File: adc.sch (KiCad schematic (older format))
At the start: 86 parts, among them J1 Conn_02x08_Odd_Even, J2 Conn_02x08_Odd_Even, J3 Conn_02x08_Odd_Even, J4 Conn_02x08_Odd_Even, J5 Conn_01x04_Male, J9 Conn_02x08_Odd_Even, U1 ADC128D818, U2 ADC128D818, U3 ADC128D818, U4 ADC128D818, U5 ADC128D818

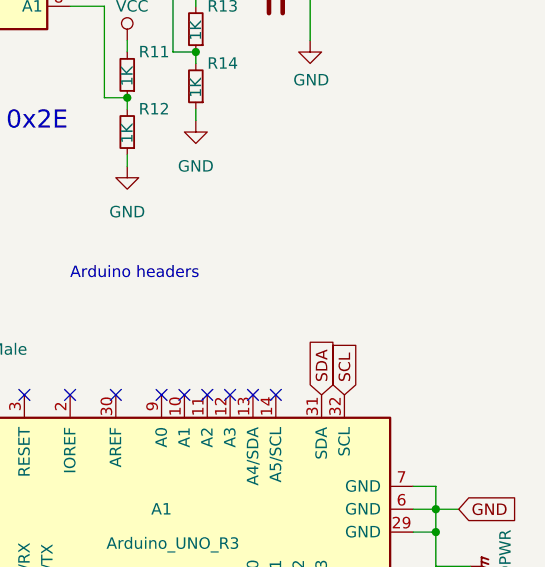
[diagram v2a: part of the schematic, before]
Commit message: add i2c pullup resistors
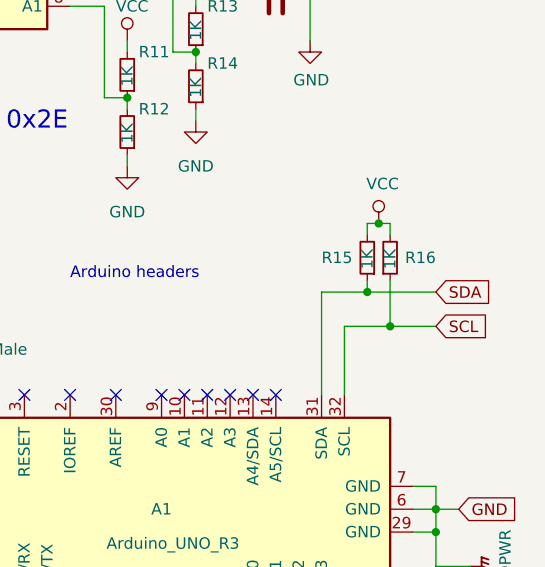
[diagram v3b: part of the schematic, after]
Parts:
- added R15, R16: 1K, Resistor_SMD:R_0805_2012Metric_Pad1.15x1.40mm_HandSolder, symbol Device:R_Small
- C1, C10, C13, C15, C17, C19, C2, C5, C7, C9: footprint Capacitor_Tantalum_SMD:CP_EIA-6032-28_Kemet-C_Pad2.25x2.35mm_HandSolder -> Capacitor_Tantalum_SMD:CP_EIA-3216-18_Kemet-A_Pad1.58x1.35mm_HandSolder
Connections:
- net SCL: now also R16.1
- net SDA: now also R15.1
- net VCC: now also R15.2, R16.2
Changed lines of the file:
@@
 	7400 5150 7400 5250
 Connection ~ 7400 5250
-Text GLabel 10300 4950 1    50   Input ~ 0
+Text GLabel 10800 4500 2    50   Input ~ 0
 SDA
-Text GLabel 10400 4950 1    50   Input ~ 0
+Text GLabel 10800 4650 2    50   Input ~ 0
 SCL
 $Comp
@@
 F 0 "C13" V 6650 5700 50  0000 L CNN
 F 1 "1U TANT C" V 6550 5400 50  0000 L CNN
-F 2 "Capacitor_Tantalum_SMD:CP_EIA-6032-28_Kemet-C_Pad2.25x2.35mm_HandSolder" H 6588 5900 50  0001 C CNN
+F 2 "Capacitor_Tantalum_SMD:CP_EIA-3216-18_Kemet-A_Pad1.58x1.35mm_HandSolder" H 6588 5900 50  0001 C CNN
 F 3 "~" H 6550 6050 50  0001 C CNN
 	1    6550 6050
@@
 F 0 "C9" H 4450 4300 50  0000 L CNN
 F 1 "1U TANT C" H 4400 4200 50  0000 L CNN
-F 2 "Capacitor_Tantalum_SMD:CP_EIA-6032-28_Kemet-C_Pad2.25x2.35mm_HandSolder" H 4938 4100 50  0001 C CNN
+F 2 "Capacitor_Tantalum_SMD:CP_EIA-3216-18_Kemet-A_Pad1.58x1.35mm_HandSolder" H 4938 4100 50  0001 C CNN
 F 3 "~" H 4900 4250 50  0001 C CNN
 	1    4900 4250
@@
 F 0 "C5" V 3100 6300 50  0000 L CNN
 F 1 "1U TANT C" V 3000 6000 50  0000 L CNN
-F 2 "Capacitor_Tantalum_SMD:CP_EIA-6032-28_Kemet-C_Pad2.25x2.35mm_HandSolder" H 3038 6500 50  0001 C CNN
+F 2 "Capacitor_Tantalum_SMD:CP_EIA-3216-18_Kemet-A_Pad1.58x1.35mm_HandSolder" H 3038 6500 50  0001 C CNN
 F 3 "~" H 3000 6650 50  0001 C CNN
 	1    3000 6650
@@
 F 0 "C1" H 900 4900 50  0000 L CNN
 F 1 "1U TANT C" H 850 4800 50  0000 L CNN
-F 2 "Capacitor_Tantalum_SMD:CP_EIA-6032-28_Kemet-C_Pad2.25x2.35mm_HandSolder" H 1388 4700 50  0001 C CNN
+F 2 "Capacitor_Tantalum_SMD:CP_EIA-3216-18_Kemet-A_Pad1.58x1.35mm_HandSolder" H 1388 4700 50  0001 C CNN
 F 3 "~" H 1350 4850 50  0001 C CNN
 	1    1350 4850
@@
 F 0 "C7" V 3500 2800 50  0000 L CNN
 F 1 "1U TANT C" V 3400 2500 50  0000 L CNN
-F 2 "Capacitor_Tantalum_SMD:CP_EIA-6032-28_Kemet-C_Pad2.25x2.35mm_HandSolder" H 3438 3000 50  0001 C CNN
+F 2 "Capacitor_Tantalum_SMD:CP_EIA-3216-18_Kemet-A_Pad1.58x1.35mm_HandSolder" H 3438 3000 50  0001 C CNN
 F 3 "~" H 3400 3150 50  0001 C CNN
 	1    3400 3150
@@
 F 0 "C2" H 1300 1400 50  0000 L CNN
 F 1 "1U TANT C" H 1250 1300 50  0000 L CNN
-F 2 "Capacitor_Tantalum_SMD:CP_EIA-6032-28_Kemet-C_Pad2.25x2.35mm_HandSolder" H 1788 1200 50  0001 C CNN
+F 2 "Capacitor_Tantalum_SMD:CP_EIA-3216-18_Kemet-A_Pad1.58x1.35mm_HandSolder" H 1788 1200 50  0001 C CNN
 F 3 "~" H 1750 1350 50  0001 C CNN
 	1    1750 1350
@@
 F 0 "C19" V 10200 2600 50  0000 L CNN
 F 1 "1U TANT C" V 10100 2300 50  0000 L CNN
-F 2 "Capacitor_Tantalum_SMD:CP_EIA-6032-28_Kemet-C_Pad2.25x2.35mm_HandSolder" H 10138 2800 50  0001 C CNN
+F 2 "Capacitor_Tantalum_SMD:CP_EIA-3216-18_Kemet-A_Pad1.58x1.35mm_HandSolder" H 10138 2800 50  0001 C CNN
 F 3 "~" H 10100 2950 50  0001 C CNN
 	1    10100 2950
@@
 F 0 "C17" H 8000 1200 50  0000 L CNN
 F 1 "1U TANT C" H 7950 1100 50  0000 L CNN
-F 2 "Capacitor_Tantalum_SMD:CP_EIA-6032-28_Kemet-C_Pad2.25x2.35mm_HandSolder" H 8488 1000 50  0001 C CNN
+F 2 "Capacitor_Tantalum_SMD:CP_EIA-3216-18_Kemet-A_Pad1.58x1.35mm_HandSolder" H 8488 1000 50  0001 C CNN
 F 3 "~" H 8450 1150 50  0001 C CNN
 	1    8450 1150
@@
 F 0 "C15" V 6950 2600 50  0000 L CNN
 F 1 "1U TANT C" V 6850 2300 50  0000 L CNN
-F 2 "Capacitor_Tantalum_SMD:CP_EIA-6032-28_Kemet-C_Pad2.25x2.35mm_HandSolder" H 6888 2800 50  0001 C CNN
+F 2 "Capacitor_Tantalum_SMD:CP_EIA-3216-18_Kemet-A_Pad1.58x1.35mm_HandSolder" H 6888 2800 50  0001 C CNN
 F 3 "~" H 6850 2950 50  0001 C CNN
 	1    6850 2950
@@
 F 0 "C10" H 4750 1200 50  0000 L CNN
 F 1 "1U TANT C" H 4700 1100 50  0000 L CNN
-F 2 "Capacitor_Tantalum_SMD:CP_EIA-6032-28_Kemet-C_Pad2.25x2.35mm_HandSolder" H 5238 1000 50  0001 C CNN
+F 2 "Capacitor_Tantalum_SMD:CP_EIA-3216-18_Kemet-A_Pad1.58x1.35mm_HandSolder" H 5238 1000 50  0001 C CNN
 F 3 "~" H 5200 1150 50  0001 C CNN
 	1    5200 1150
@@
 NoConn ~ 9100 5950
 NoConn ~ 9000 5950
+$Comp
+L Device:R_Small R15
+U 1 1 5C4E408F
+P 10500 4350
+F 0 "R15" H 10700 4350 50  0000 R CNN
+F 1 "1K" V 10500 4400 50  0000 R CNN
+F 2 "Resistor_SMD:R_0805_2012Metric_Pad1.15x1.40mm_HandSolder" H 10500 4350 50  0001 C CNN
+F 3 "~" H 10500 4350 50  0001 C CNN
+	1    10500 4350
+	-1   0    0    1
+$EndComp
+Wire Wire Line
+	10400 4650 10600 4650
+Wire Wire Line
+	10800 4500 10500 4500
+Wire Wire Line
+	10400 4650 10400 4950
+Wire Wire Line
+	10300 4500 10300 4950
+$Comp
+L power:VCC #PWR044
+U 1 1 5C63A4BA
+P 10550 4200
+F 0 "#PWR044" H 10550 4050 50  0001 C CNN
+F 1 "VCC" H 10567 4373 50  0000 C CNN
+F 2 "" H 10550 4200 50  0001 C CNN
+F 3 "" H 10550 4200 50  0001 C CNN
+	1    10550 4200
+	1    0    0    -1
+$EndComp
+$Comp
+L Device:R_Small R16
+U 1 1 5C63AD89
+P 10600 4350
+F 0 "R16" H 10800 4350 50  0000 R CNN
+F 1 "1K" V 10600 4400 50  0000 R CNN
+F 2 "Resistor_SMD:R_0805_2012Metric_Pad1.15x1.40mm_HandSolder" H 10600 4350 50  0001 C CNN
+F 3 "~" H 10600 4350 50  0001 C CNN
+	1    10600 4350
+	1    0    0    1
+$EndComp
+Wire Wire Line
+	10500 4450 10500 4500
+Connection ~ 10500 4500
+Wire Wire Line
+	10500 4500 10300 4500
+Wire Wire Line
+	10600 4450 10600 4650
+Connection ~ 10600 4650
+Wire Wire Line
+	10600 4650 10800 4650
+Wire Wire Line
+	10550 4200 10500 4200
+Wire Wire Line
+	10500 4200 10500 4250
+Wire Wire Line
+	10550 4200 10600 4200
+Wire Wire Line
+	10600 4200 10600 4250
+Connection ~ 10550 4200
 $EndSCHEMATC

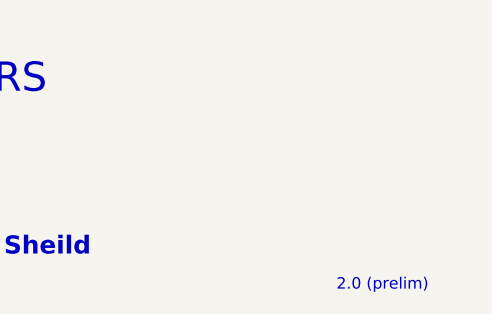
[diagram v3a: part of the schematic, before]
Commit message: mark schematic as V2 final
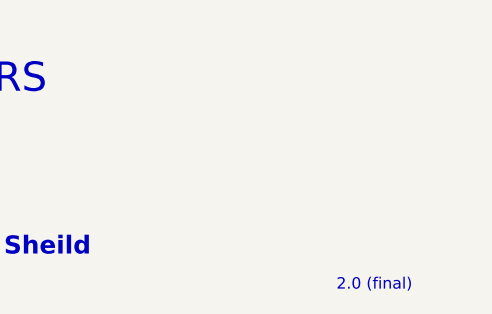
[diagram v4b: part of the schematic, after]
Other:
- note added: "2.0 (final)"
- note removed: "2.0 (prelim)"
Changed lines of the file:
@@
 2018 Nov 29
 Text Notes 10600 7650 0    50   ~ 0
-2.0 (prelim)
+2.0 (final)
 Text Notes 7000 7000 0    128  ~ 0
 Property  of Team OTheRS\nJacob Killelea

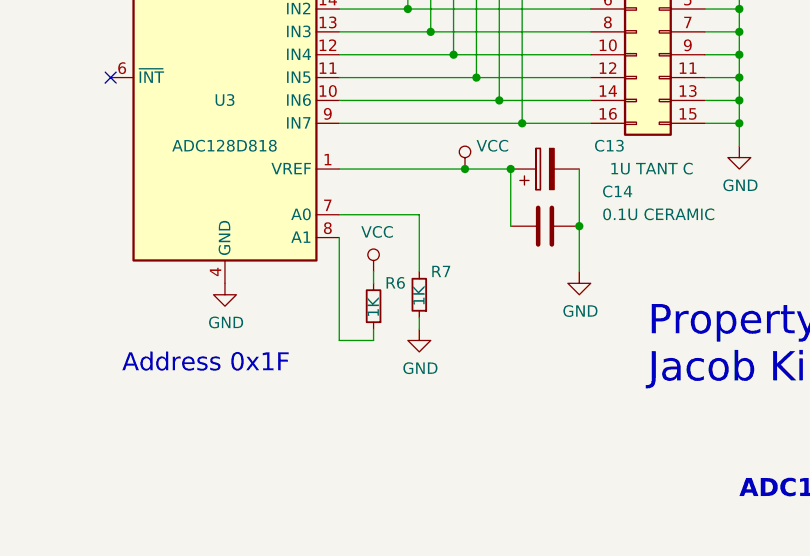
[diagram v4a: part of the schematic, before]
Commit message: update trace width after ITLL CNC cutting and correct error causing chip 0x1F to show up as 0x35
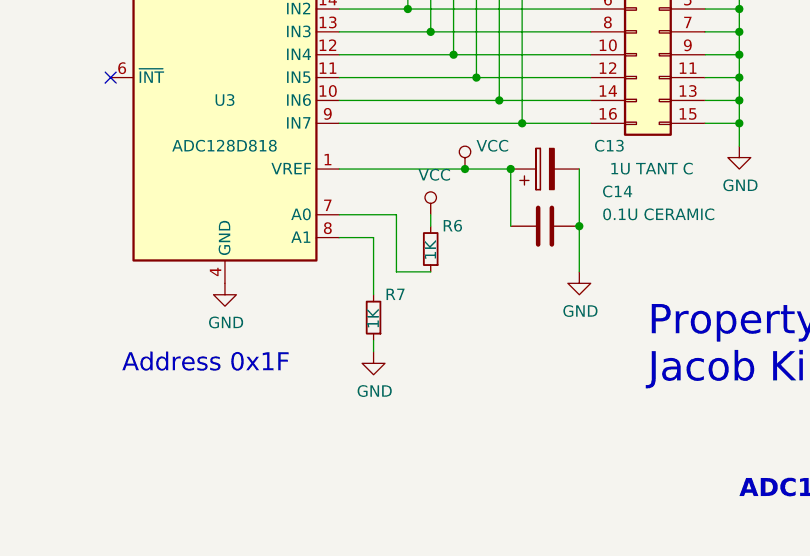
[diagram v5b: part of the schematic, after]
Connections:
- net at U3.7 (A0): now also R6.1; no longer R7.2
- net at U3.8 (A1): now also R7.2; no longer R6.1
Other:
- moved on the sheet: R6, R7
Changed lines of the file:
@@
 L Device:R_Small R7
 U 1 1 5CDACB2D
-P 6000 6600
-F 0 "R7" H 5950 6500 50  0000 R CNN
-F 1 "1K" V 6000 6650 50  0000 R CNN
-F 2 "Resistor_SMD:R_0805_2012Metric_Pad1.15x1.40mm_HandSolder" H 6000 6600 50  0001 C CNN
-F 3 "~" H 6000 6600 50  0001 C CNN
-	1    6000 6600
+P 5800 6700
+F 0 "R7" H 5750 6600 50  0000 R CNN
+F 1 "1K" V 5800 6750 50  0000 R CNN
+F 2 "Resistor_SMD:R_0805_2012Metric_Pad1.15x1.40mm_HandSolder" H 5800 6700 50  0001 C CNN
+F 3 "~" H 5800 6700 50  0001 C CNN
+	1    5800 6700
 	-1   0    0    1
 $EndComp
@@
 L power:GND #PWR016
 U 1 1 5C457890
-P 6000 6750
-F 0 "#PWR016" H 6000 6500 50  0001 C CNN
-F 1 "GND" H 6005 6577 50  0000 C CNN
-F 2 "" H 6000 6750 50  0001 C CNN
-F 3 "" H 6000 6750 50  0001 C CNN
-	1    6000 6750
-	1    0    0    -1
-$EndComp
-Wire Wire Line
-	6000 6700 6000 6750
-Wire Wire Line
-	5650 6250 6000 6250
-Wire Wire Line
-	6000 6250 6000 6500
+P 5800 6850
+F 0 "#PWR016" H 5800 6600 50  0001 C CNN
+F 1 "GND" H 5805 6677 50  0000 C CNN
+F 2 "" H 5800 6850 50  0001 C CNN
+F 3 "" H 5800 6850 50  0001 C CNN
+	1    5800 6850
+	1    0    0    -1
+$EndComp
+Wire Wire Line
+	5800 6800 5800 6850
 $Comp
 L power:VCC #PWR012
 U 1 1 5C4B3FE4
-P 5800 6500
-F 0 "#PWR012" H 5800 6350 50  0001 C CNN
-F 1 "VCC" H 5817 6673 50  0000 C CNN
-F 2 "" H 5800 6500 50  0001 C CNN
-F 3 "" H 5800 6500 50  0001 C CNN
-	1    5800 6500
+P 6050 6250
+F 0 "#PWR012" H 6050 6100 50  0001 C CNN
+F 1 "VCC" H 6067 6423 50  0000 C CNN
+F 2 "" H 6050 6250 50  0001 C CNN
+F 3 "" H 6050 6250 50  0001 C CNN
+	1    6050 6250
 	1    0    0    -1
 $EndComp
@@
 L Device:R_Small R6
 U 1 1 5C4B413F
-P 5800 6650
-F 0 "R6" H 5750 6550 50  0000 R CNN
-F 1 "1K" V 5800 6700 50  0000 R CNN
-F 2 "Resistor_SMD:R_0805_2012Metric_Pad1.15x1.40mm_HandSolder" H 5800 6650 50  0001 C CNN
-F 3 "~" H 5800 6650 50  0001 C CNN
-	1    5800 6650
-	-1   0    0    1
-$EndComp
-Wire Wire Line
-	5800 6500 5800 6550
-Wire Wire Line
-	5800 6750 5800 6800
-Wire Wire Line
-	5800 6800 5650 6800
-Wire Wire Line
-	5650 6800 5650 6350
+P 6050 6400
+F 0 "R6" H 6000 6300 50  0000 R CNN
+F 1 "1K" V 6050 6450 50  0000 R CNN
+F 2 "Resistor_SMD:R_0805_2012Metric_Pad1.15x1.40mm_HandSolder" H 6050 6400 50  0001 C CNN
+F 3 "~" H 6050 6400 50  0001 C CNN
+	1    6050 6400
+	-1   0    0    1
+$EndComp
+Wire Wire Line
+	6050 6250 6050 6300
 Text Notes 4700 6950 0    79   ~ 0
 Address 0x1F
@@
 	10600 4200 10600 4250
 Connection ~ 10550 4200
+Wire Wire Line
+	5650 6350 5800 6350
+Wire Wire Line
+	5800 6350 5800 6600
+Wire Wire Line
+	5650 6250 5900 6250
+Wire Wire Line
+	5900 6250 5900 6500
+Wire Wire Line
+	5900 6500 6050 6500
 $EndSCHEMATC
